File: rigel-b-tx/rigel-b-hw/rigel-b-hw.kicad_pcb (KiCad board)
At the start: 4 copper layers, 35 x 20 mm, 44 parts, among them IC1 BALFHB-WL-02D3, J1 Conn_01x03_Pin, J3 Conn_01x03_Pin, U1 STM32WLE5C8Ux, U2 XC6206P332MR, U3 CH340X, U4 TYPE-C_16PIN_2MD(073), U5 X1G004131004200, U6 KH-SMA-K513-G

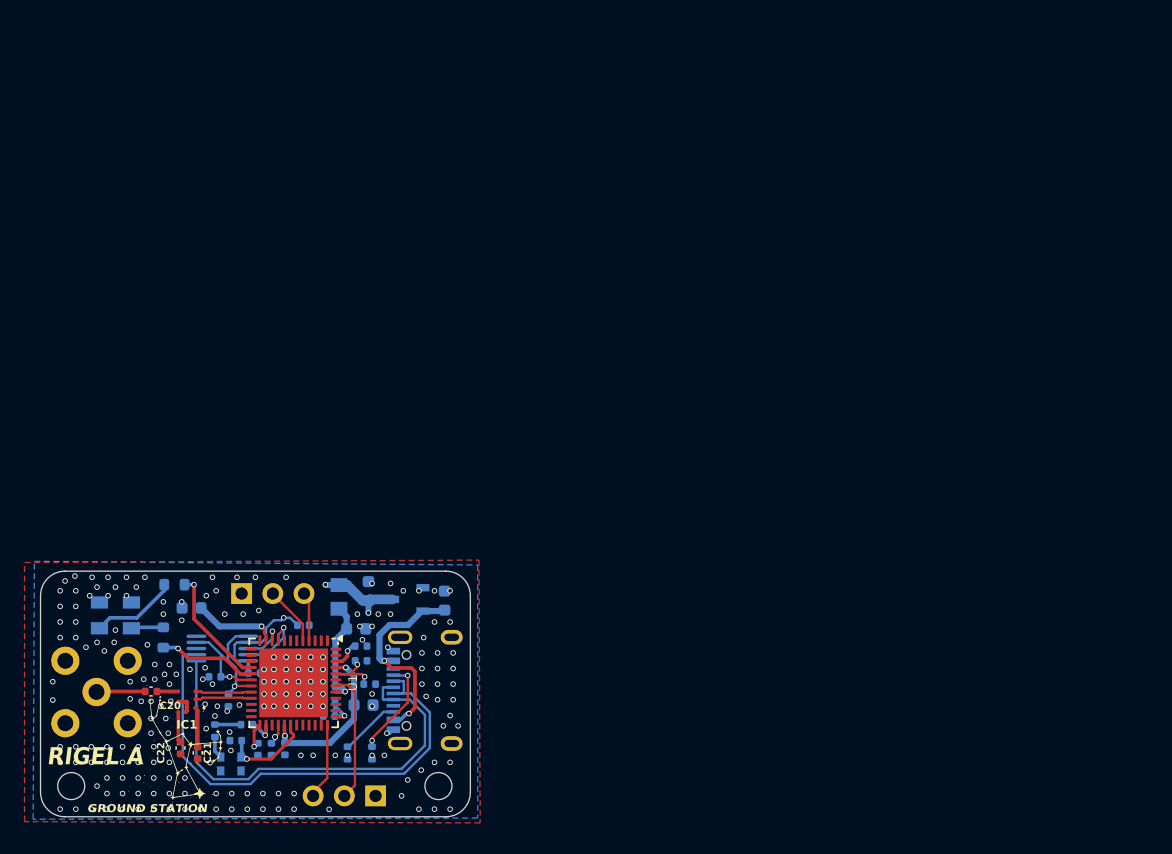
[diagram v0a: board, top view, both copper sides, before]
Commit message: PCB Layout ALMOST done
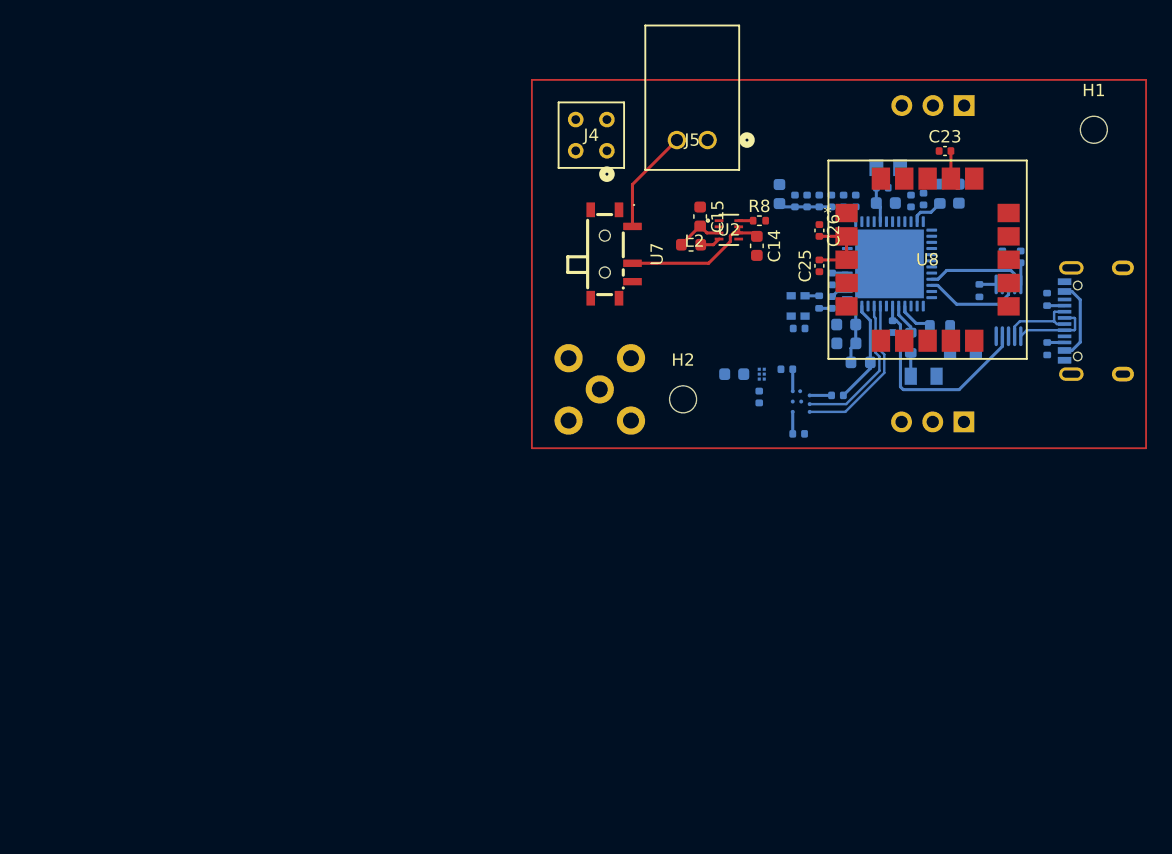
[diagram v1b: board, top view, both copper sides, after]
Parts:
- removed G*** (x2): LOGO, jlc:orion-logo
- added C23: 100nF, Capacitor_SMD:C_0402_1005Metric, F.Cu at (173.7, 65.8)
- added C24: 100nF, Capacitor_SMD:C_0402_1005Metric, B.Cu at (158.5, 85.8)
- added C25: 100nF, Capacitor_SMD:C_0402_1005Metric, F.Cu at (163.4, 75.1)
- added C26: 100nF, Capacitor_SMD:C_0402_1005Metric, F.Cu at (163.4, 72.3)
- added C27: 47nF, Capacitor_SMD:C_0603_1608Metric, B.Cu at (165.6, 79.9)
- added C28: 68pF, Capacitor_SMD:C_0603_1608Metric, B.Cu at (165.6, 81.5)
- added C29: 4.7uF, Capacitor_SMD:C_0402_1005Metric, B.Cu at (171.9, 69.7)
- added C30: 0.47uF, Capacitor_SMD:C_0603_1608Metric, B.Cu at (174.8, 69.3)
- added J4: BCS-102-L-D-TE, jlc:CON4_2X2_TU_BCS_SAI, F.Cu at (144.8, 64.5)
- added J5: S2B-XH-A, jlc:CONN_S2B-XH-A_JST, F.Cu at (154.3, 64.9)
- added L2: 2.2uH, Inductor_SMD:L_0603_1608Metric, F.Cu at (153.0, 73.4)
- added L3: 47nH, Inductor_SMD:L_0603_1608Metric, B.Cu at (166.8, 83.0)
- added L4: 15uH, Inductor_SMD:L_0603_1608Metric, B.Cu at (173.2, 69.3)
- added R8: 27.4k, Resistor_SMD:R_0402_1005Metric, F.Cu at (158.5, 71.5)
- added U7: MSK12C02-HB, jlc:SW-TH_MSK12C02-HB-1, F.Cu at (146.5, 74.2)
- added U8: SAM-M10Q-00B, jlc:SAM-M10Q_UBL, F.Cu at (172.2, 74.6)
- added U9: BGS12WN6E6327XTSA1, jlc:PG-TSNP-6-10_INF, B.Cu at (158.7, 84.0)
- C1: value 0.47uF -> 68pF
- C14: value 1uF -> 4.7uF; moved to F.Cu
- C15: value 1uF -> 22uF; moved to F.Cu
- C20: value 68pF -> 0; moved to B.Cu
- C21: value 68pF -> 100pF; moved to B.Cu
- C22, IC1, U1: moved to B.Cu
- U2: value XC6206P332MR -> TPS629206DRLR; footprint jlc:SOT-23-3_L2.9-W1.6-P1.90-LS2.8-BR -> jlc:SOT5X3-8_DRL_TEX; moved to F.Cu
- moved H1 75.5 mm to (185.8, 64.1)
- moved J1 73.9 mm to (175.2, 62.1)
- moved LED1 73.6 mm to (175.1, 82.0), turned to 180 degrees
- moved C10 71.0 mm to (179.8, 74.4), turned to -90 degrees
- moved U3 69.7 mm to (178.8, 78.8), turned to 180 degrees
- moved R3 69.6 mm to (176.4, 77.2)
- moved LED2 67.4 mm to (171.9, 84.1), turned to 180 degrees
- moved R1 66.2 mm to (182.0, 77.9), turned to -90 degrees
- moved R6 65.8 mm to (173.2, 80.0), turned to 0 degrees
- moved R2 65.8 mm to (182.0, 81.9)
- moved R5 65.4 mm to (170.9, 81.4), turned to -90 degrees
- moved C12 64.3 mm to (178.3, 74.4), turned to -90 degrees
- moved C7 63.8 mm to (164.4, 69.9), turned to 90 degrees
- moved C4 62.5 mm to (161.4, 69.9), turned to 90 degrees
- moved U4 62.4 mm to (185.8, 79.6)
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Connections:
- C1 pad 1: GND -> Net-(U9-RFIN)
- C1 pad 2: +1V5 -> Net-(U6-IN)
- C14 pad 1: +3.3V -> Net-(U2-EN)
- C15 pad 1: +5V -> GND
- C15 pad 2: GND -> +3.3V
- C20 pad 1: Net-(IC1-RFI_IN) -> GND
- C20 pad 2: Net-(U6-IN) -> Net-(IC1-RFI_IN)
- C21 pad 2: GND -> Net-(U1-RFO_HP)
- C22 pad 1: Net-(IC1-RFO_OUT) -> Net-(U9-RF2)
- C22 pad 2: GND -> Net-(IC1-RFO_OUT)
- U1 pad 23: unconnected-(U1-RFO_HP-Pad23) -> Net-(U1-RFO_HP)
- U1 pad 24: unconnected-(U1-VR_PA-Pad24) -> Net-(U1-VR_PA)
- U1 pad 38: unconnected-(U1-PC13-Pad38) -> Net-(U1-PC13)
- U1 pad 47: unconnected-(U1-VLXSMPS-Pad47) -> Net-(U1-VLXSMPS)
- U2 pad 2: +5V -> unconnected-(U2-PG-Pad2)
- U4 pad 11: +5V -> Net-(U4-VBUS-Pad11)
- U4 pad 2: +5V -> Net-(U4-VBUS-Pad11)
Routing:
- net USBD-: track 40.8 -> 6.72 mm
- net USBD+: track 36.8 -> 6.41 mm
- net +5V: track 17.7 -> 0.00 mm, vias 2 -> 0
- net +3.3V: track 40.5 -> 23.3 mm, vias 11 -> 0
- net Net-(U2-EN): track 0.00 -> 12.0 mm
- net /RESET: track 6.91 -> 17.7 mm, vias 1 -> 0
- net /JTCK/SWCLK: track 10.6 -> 0.00 mm
- net +1V5: track 13.1 -> 2.78 mm, vias 2 -> 0
- net Net-(J5-Pad2): track 0.00 -> 8.53 mm
- net Net-(U1-RFO_HP): track 0.00 -> 8.47 mm
- net /RFI+: track 4.63 -> 13.0 mm
- net /RFI-: track 4.64 -> 12.2 mm
- net /PB0-VDD_TCXO: track 7.42 -> 0.00 mm, vias 1 -> 0
- net /TIM1_CH1_LED_1: track 9.88 -> 2.99 mm, vias 1 -> 0
- net Net-(U4-CC1): track 8.14 -> 1.43 mm, vias 2 -> 0
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- removed copper zone on B.Cu, net GND
- removed copper zone on F.Cu, net GND
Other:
- board outline removed
- board text removed: "AD ASTRA"
- board text removed: "GND SWCLK SWDIO"
- board text removed: "GROUND STATION"
- board text removed: "JLCJLCJLCJLC"
- board text removed: "RIGEL A"
- board text removed: "STAT INFO"
- board text removed: "SWD"
- board text removed: "TX RX GND"

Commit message: PCB Layout
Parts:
- removed J1, J3: Conn_01x03_Pin, Connector_PinSocket_2.54mm:PinSocket_1x03_P2.54mm_Vertical
- added ?: , , F.Cu at (143.6, 86.5)
- added ?: , , F.Cu at (178.4, 63.5)
- moved H1 54.5 mm to (131.4, 68.1)
- moved H2 22.6 mm to (131.7, 76.8)
- moved U6 5.48 mm to (151.0, 85.4), turned to 90 degrees
- moved C11 2.70 mm to (171.9, 67.4)
- moved L1 2.33 mm to (166.7, 67.1), turned to 0 degrees
- moved C12 2.07 mm to (180.3, 74.0), turned to 180 degrees
- moved C29 1.95 mm to (170.9, 68.0)
- moved C3 1.06 mm to (167.7, 69.4), turned to 90 degrees
- moved LED2 0.98 mm to (172.8, 84.4)
- moved R5 0.87 mm to (171.7, 81.2)
- moved C10 0.82 mm to (180.3, 75.0), turned to 180 degrees
- moved R6 0.80 mm to (174.0, 80.0)
- moved C16 0.75 mm to (169.0, 69.3), turned to -90 degrees
- moved C13 0.61 mm to (169.8, 80.5)
- moved C2 0.51 mm to (163.9, 76.2)
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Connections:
- U1 pad 36: /JTMS/SWDIO -> unconnected-(U1-PA13-Pad36)
- U1 pad 42: /JTCK/SWCLK -> unconnected-(U1-PA14-Pad42)
- U8 pad 13: unconnected-(U8-TXD-Pad13) -> /USART1_RX
- U8 pad 14: unconnected-(U8-RXD-Pad14) -> /USART1_TX
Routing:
- net +3.3V: track 23.3 -> 88.7 mm, vias 0 -> 8
- net Net-(U4-VBUS-Pad11): track 6.57 -> 53.2 mm, vias 0 -> 1
- net +1V5: track 2.78 -> 35.3 mm
- net /BOOT0: track 1.37 -> 25.6 mm, vias 0 -> 2
- net Net-(U1-PC13): track 0.00 -> 17.8 mm, vias 0 -> 2
- net /USART1_TX: track 0.00 -> 13.4 mm, vias 0 -> 1
- net /USART1_RX: track 0.00 -> 13.3 mm, vias 0 -> 1
- net /PB0-VDD_TCXO: track 0.00 -> 12.0 mm, vias 0 -> 2
- net GND: track 0.00 -> 7.02 mm, vias 0 -> 3
- net Net-(U6-IN): track 0.00 -> 5.31 mm
- net /RESET: track 17.7 -> 13.1 mm
- net Net-(IC1-RFI_IN): track 1.79 -> 5.35 mm
- net /USART2_TX: track 8.00 -> 9.77 mm
- net Net-(U9-RF2): track 0.00 -> 1.35 mm
- net /USART2_RX: track 8.04 -> 8.85 mm
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- added copper zone on In2.Cu, net +1V5
- added copper zone on In1.Cu, net +3.3V
- added copper zone on B.Cu, net GND
- added copper zone on F.Cu, net GND
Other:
- board outline added: 50.1 x 30.1 mm

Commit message: RF Switch finalized
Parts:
- U9: value BGS12WN6E6327XTSA1 -> PE42520C-Z; footprint jlc:PG-TSNP-6-10_INF -> jlc:QFN_2520C-Z_PSM
- moved U9 12.3 mm to (164.3, 94.9)
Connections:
- C1 pad 1: Net-(U9-RFIN) -> Net-(U9-RFC)
- U9 pad 1: Net-(U9-RF2) -> GND
- U9 pad 2: GND -> Net-(IC1-RFI_IN)
- U9 pad 3: Net-(IC1-RFI_IN) -> GND
- U9 pad 4: +3.3V -> GND
- U9 pad 5: Net-(U9-RFIN) -> GND
- U9 pad 6: Net-(U1-PC13) -> GND
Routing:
- net Net-(IC1-RFI_IN): track 5.35 -> 1.79 mm
- net Net-(U9-RF2): track 1.35 -> 0.00 mm
- net Net-(U1-PC13): track 17.8 -> 16.4 mm
- net +3.3V: track 88.7 -> 87.7 mm

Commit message: New Switch
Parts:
- removed U9: PE42520C-Z, jlc:QFN_2520C-Z_PSM
- added C31: 22pF, Capacitor_SMD:C_0402_1005Metric, B.Cu at (165.7, 94.7)
- added U10: 4259-63, jlc:SC-70-6_PSM, B.Cu at (167.3, 92.6)

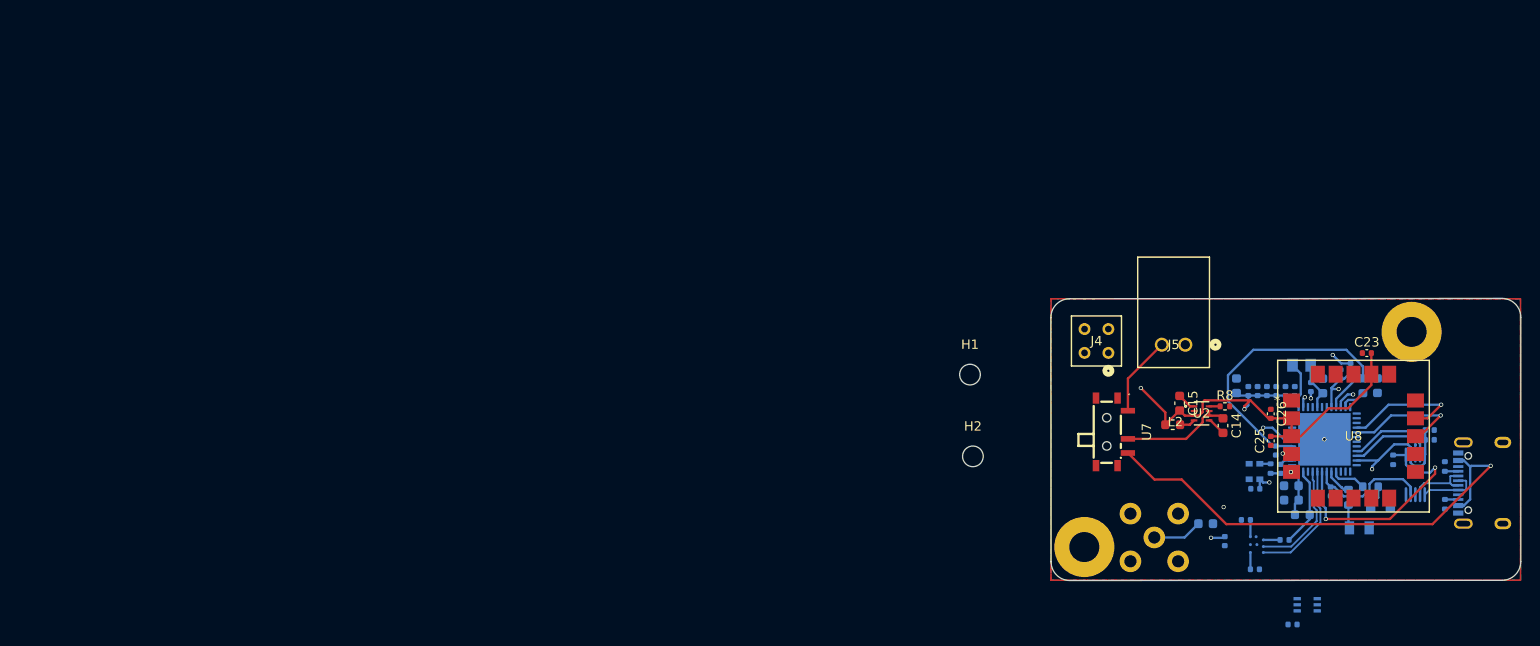
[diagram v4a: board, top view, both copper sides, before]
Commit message: Added Datasheets
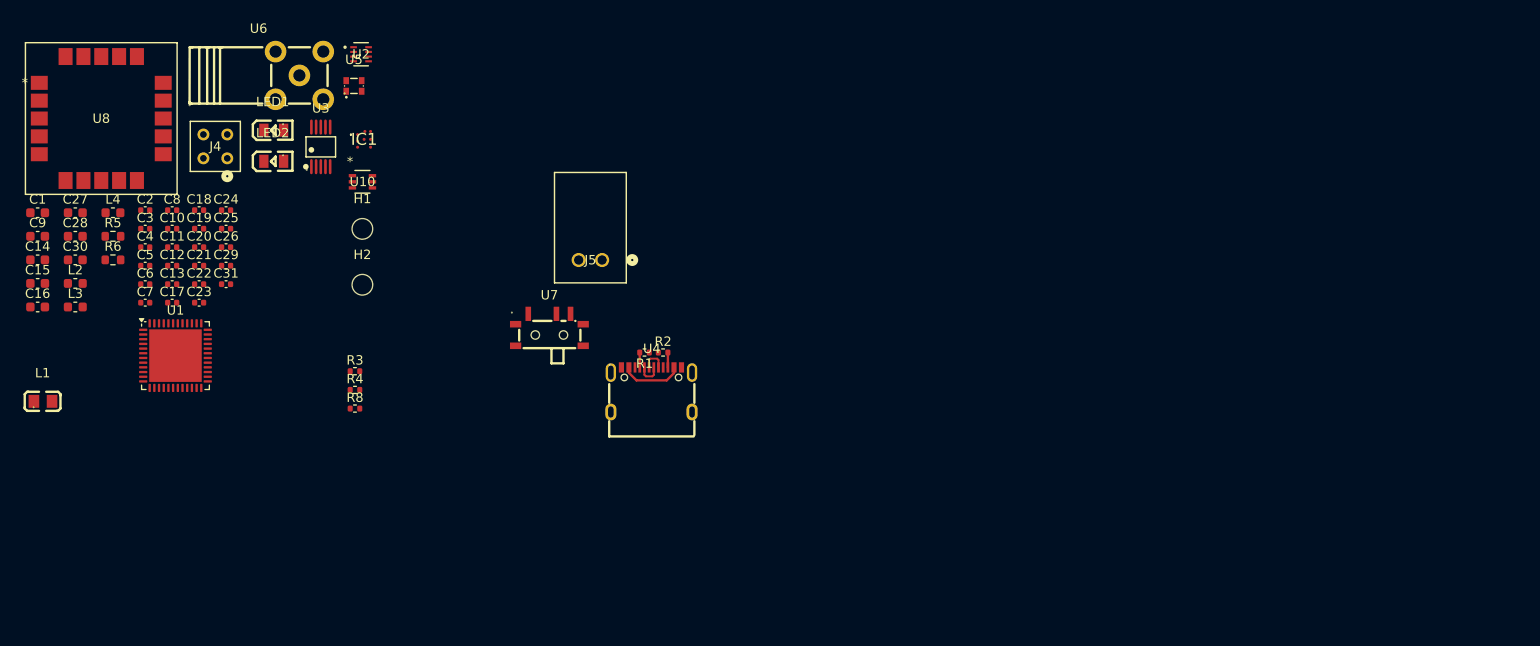
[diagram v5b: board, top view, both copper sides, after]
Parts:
- removed ? (x2): , 
- C1, C10, C11, C12, C13, C16, C17, C18, C19, C2, C20, C21, C22, C24, C27, C28, C29, C3, C30, C31, C4, C5, C6, C7, C8, C9, IC1, L1, L3, L4, LED1, LED2, R1, R2, R3, R4, R5, R6, U1, U10, U3, U4, U5, U6: moved to F.Cu
- moved C30 139.3 mm to (36.1, 55.9), turned to 0 degrees
- moved U8 137.6 mm to (38.8, 40.8)
- moved C16 137.1 mm to (32.1, 60.9), turned to 0 degrees
- moved R6 136.1 mm to (40.1, 55.9)
- moved C10 135.8 mm to (46.4, 52.5), turned to 0 degrees
- moved C12 135.1 mm to (46.4, 56.5), turned to 0 degrees
- moved R5 134.5 mm to (40.1, 53.4), turned to 0 degrees
- moved L4 134.4 mm to (40.1, 50.8), turned to 0 degrees
- moved L1 134.1 mm to (32.6, 70.9)
- moved C27 132.7 mm to (36.1, 50.8)
- moved L3 132.6 mm to (36.1, 60.9), turned to 0 degrees
- moved C28 132.5 mm to (36.1, 53.4)
- moved C1 128.7 mm to (32.1, 50.8), turned to 0 degrees
- moved C9 128.7 mm to (32.1, 53.4), turned to 0 degrees
- moved C14 127.5 mm to (32.1, 55.9), turned to 0 degrees
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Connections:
- U1 pad 1: unconnected-(U1-PB3-Pad1) -> Data 2
- U1 pad 31: unconnected-(U1-PB2-Pad31) -> Data 1
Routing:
- net +3.3V: track 87.7 -> 0.00 mm, vias 8 -> 0
- net Net-(U4-VBUS-Pad11): track 53.2 -> 6.63 mm, vias 1 -> 0
- net +1V5: track 35.3 -> 0.00 mm
- net /BOOT0: track 25.6 -> 0.00 mm, vias 2 -> 0
- net Net-(U1-PC13): track 16.4 -> 0.00 mm, vias 2 -> 0
- net /USART1_TX: track 13.4 -> 0.00 mm, vias 1 -> 0
- net /USART1_RX: track 13.3 -> 0.00 mm, vias 1 -> 0
- net /RESET: track 13.1 -> 0.00 mm
- net /RFI+: track 13.0 -> 0.00 mm
- net /RFI-: track 12.2 -> 0.00 mm
- net Net-(U2-EN): track 12.0 -> 0.00 mm
- net /PB0-VDD_TCXO: track 12.0 -> 0.00 mm, vias 2 -> 0
- net /USART2_TX: track 9.77 -> 0.00 mm
- net /USART2_RX: track 8.85 -> 0.00 mm
- net Net-(J5-Pad2): track 8.53 -> 0.00 mm
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- removed copper zone on In2.Cu, net +1V5
- removed copper zone on In1.Cu, net +3.3V
- removed copper zone on In2.Cu, net +3.3V
- removed copper zone on B.Cu, net GND
- removed copper zone on F.Cu, net GND
- removed copper zone on In1.Cu, net GND
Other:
- board outline removed
- board text removed: "{ "ViaStitching": "0.2", "stitch_zone_0": { "HSpacing": "1.16", "VSpacing": "1.16", "Clearance": "2", "Randomize": false } }"

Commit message: Began some traces
Waiting on Polaris. Started tracing individual systems.
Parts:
- moved R5 223.5 mm to (261.9, 26.2)
- moved R6 223.4 mm to (261.9, 29.5)
- moved LED2 209.2 mm to (265.6, 26.2), turned to 180 degrees
- moved LED1 208.7 mm to (265.6, 29.5), turned to 180 degrees
- moved C18 158.6 mm to (207.8, 48.4)
- moved C1 158.1 mm to (189.6, 64.3)
- moved C17 154.7 mm to (200.6, 48.3)
- moved R4 141.7 mm to (205.9, 48.4)
- moved U5 140.8 mm to (205.7, 53.0)
- moved U6 123.9 mm to (180.6, 64.5)
- moved C22 118.2 mm to (166.3, 41.6), turned to -90 degrees
- moved C20 117.5 mm to (166.3, 44.2), turned to 90 degrees
- moved C21 113.0 mm to (161.3, 41.9), turned to 90 degrees
- moved U8 103.2 mm to (139.2, 64.6)
- moved IC1 97.0 mm to (163.8, 42.4)
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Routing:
- net +3.3V: track 0.00 -> 15.4 mm
- net Net-(U4-VBUS-Pad11): track 6.63 -> 13.1 mm
- net Net-(U2-EN): track 0.00 -> 6.18 mm
- net Net-(J5-Pad2): track 0.00 -> 4.76 mm
- net GND: track 0.00 -> 3.52 mm, vias 0 -> 3
- net Net-(U2-SW): track 0.00 -> 1.98 mm
- net Net-(IC1-RFI_IN): track 0.00 -> 1.81 mm
- net Net-(IC1-RFO_OUT): track 0.00 -> 1.79 mm
- net Net-(IC1-RFO_IN): track 0.00 -> 1.79 mm
- net Net-(LED1-A): track 0.00 -> 1.78 mm
- net Net-(LED2-A): track 0.00 -> 1.77 mm
- net Net-(U2-MODE/S-CONF): track 0.00 -> 1.22 mm
- net /BOOT0: track 0.00 -> 0.86 mm
